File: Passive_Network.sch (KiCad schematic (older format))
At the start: 140 parts, among them J18 CONN_01X03, J19 CONN_01X03, J20 CONN_01X08, SW2 SW_Rotary3x4, X1 P7002SCLRP, X2 P7002SCLRP, X3 P7002SCLRP, X4 P7002SCLRP, X5 P7002SCLRP, X6 P7002SCLRP

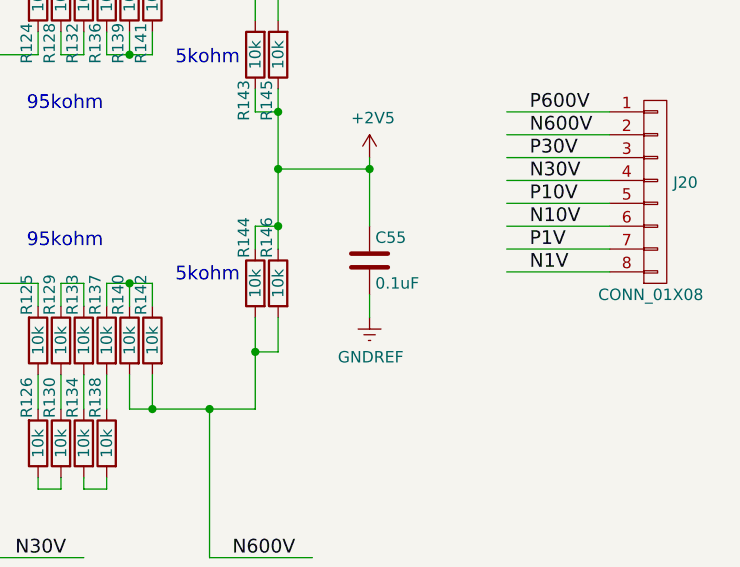
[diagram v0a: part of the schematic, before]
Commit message: 전해콘덴서 foot print 변경
전해 콘덴서 변경
Bypass 콘데서 OPAMP에 추가 하여야 함
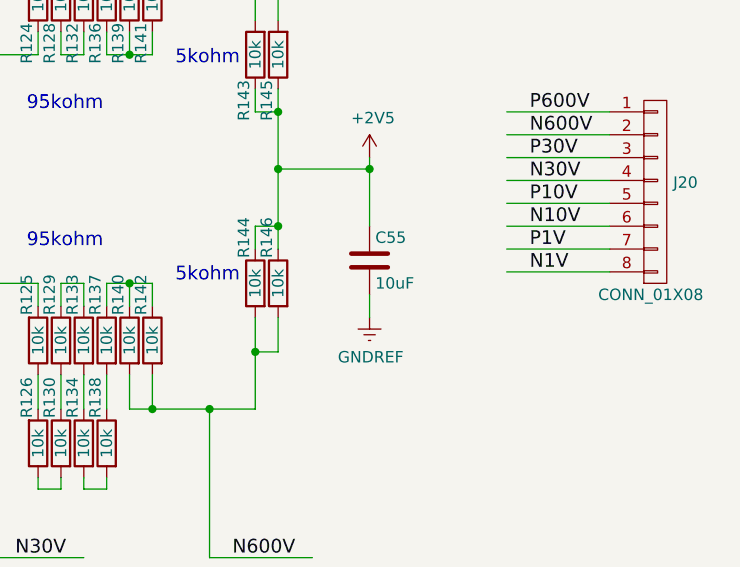
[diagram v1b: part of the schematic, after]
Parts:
- C55: value 0.1uF -> 10uF
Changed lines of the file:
@@
 P 9400 3300
 F 0 "C55" H 9425 3400 50  0000 L CNN
-F 1 "0.1uF" H 9425 3200 50  0000 L CNN
+F 1 "10uF" H 9425 3200 50  0000 L CNN
 F 2 "Capacitors_SMD:C_1210_HandSoldering" H 9438 3150 50  0001 C CNN
 F 3 "" H 9400 3300 50  0001 C CNN

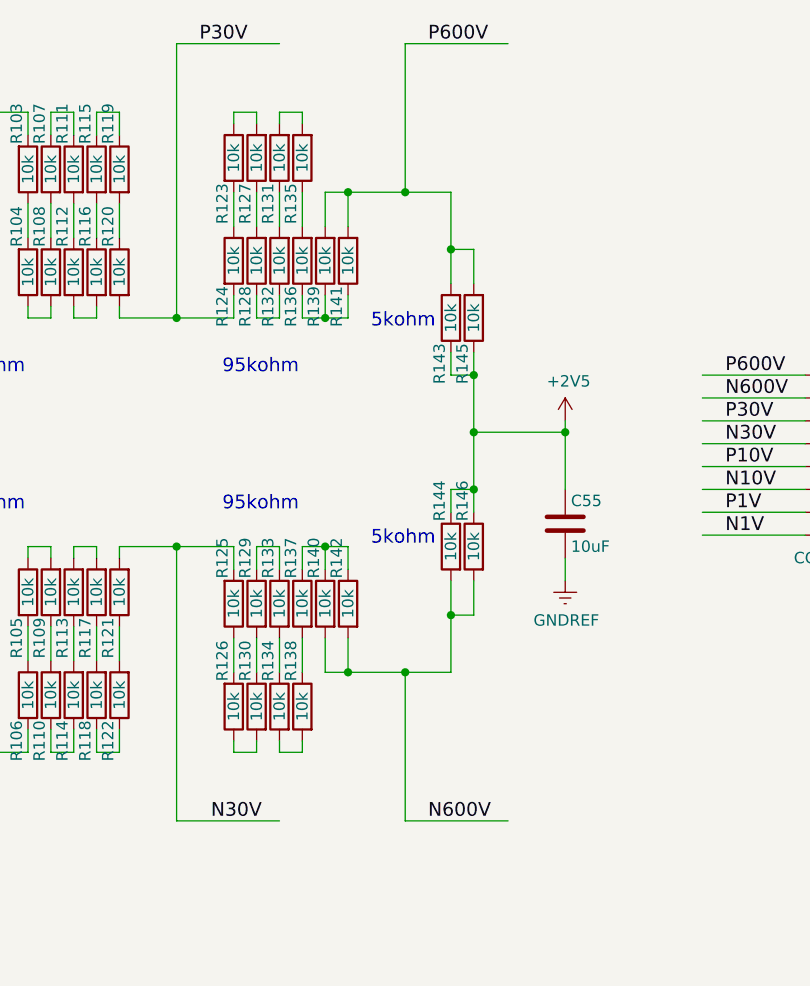
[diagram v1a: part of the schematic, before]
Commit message: 2차 PCB 1차 수정
1. ADR455 Vcc V12 수정
2. DCDC 입력전압 변경
3. Bypass 콘덴서 C66, C67 추가
4. SOIC 방향 표시
5. TLV431 PADS 변경
6. AQV258 Pin3 --> Pin2
7. 전해콘덴서 방향추가
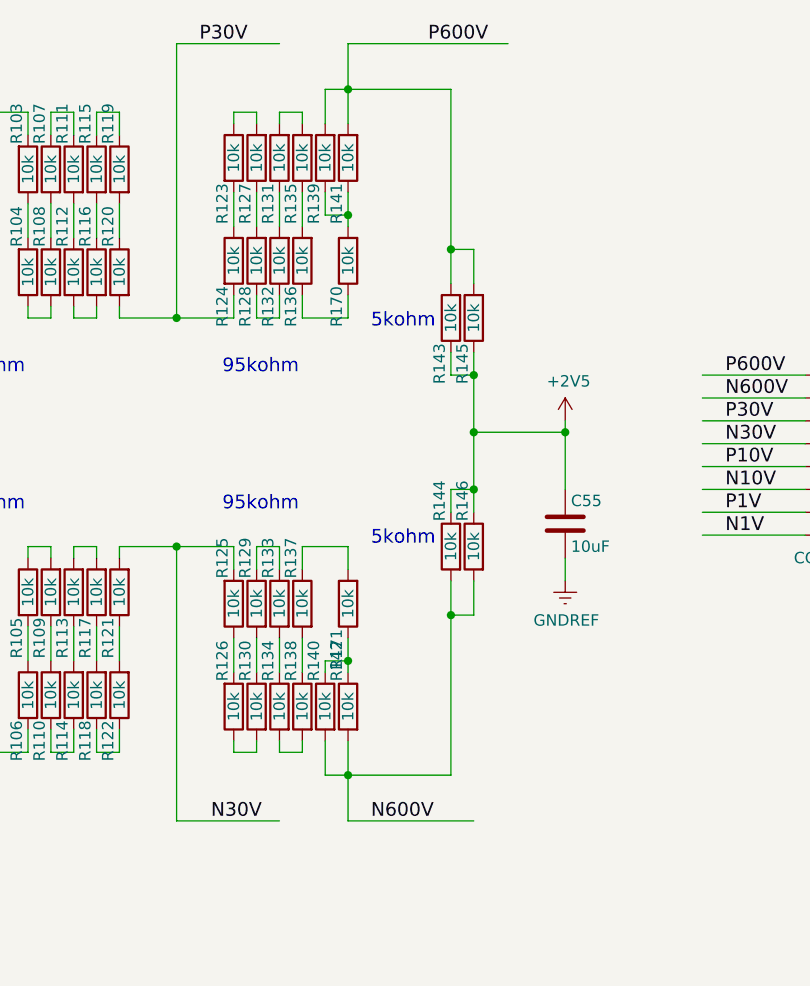
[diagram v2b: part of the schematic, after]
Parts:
- added R170, R171: 10k, Resistors_SMD:R_0805_HandSoldering, symbol R
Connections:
- wire segments 327 -> 329
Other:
- moved on the sheet: R139, R140, R141, R142
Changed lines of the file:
@@
 P30V
 Wire Wire Line
-	8700 1850 8700 1200
-Wire Wire Line
-	8700 1200 9150 1200
+	8450 1200 9150 1200
 Text Label 8800 1200 0    60   ~ 0
 P600V
@@
 Text Label 7850 4600 0    60   ~ 0
 N30V
-Text Label 8800 4600 0    60   ~ 0
+Text Label 8550 4600 0    60   ~ 0
 N600V
 Text Label 6300 4600 0    60   ~ 0
@@
 Text Label 6750 5750 0    60   ~ 0
 Monitor
-Connection ~ 8700 1850
 $Comp
 L C C55
@@
 L R R139
 U 1 1 5B0CFCAF
-P 8350 2150
-F 0 "R139" V 8400 2350 50  0000 C CNN
-F 1 "10k" V 8350 2150 50  0000 C CNN
-F 2 "Resistors_SMD:R_0805_HandSoldering" V 8280 2150 50  0001 C CNN
-F 3 "" H 8350 2150 50  0001 C CNN
-	1    8350 2150
+P 8350 1700
+F 0 "R139" V 8400 1900 50  0000 C CNN
+F 1 "10k" V 8350 1700 50  0000 C CNN
+F 2 "Resistors_SMD:R_0805_HandSoldering" V 8280 1700 50  0001 C CNN
+F 3 "" H 8350 1700 50  0001 C CNN
+	1    8350 1700
 	-1   0    0    1
 $EndComp
@@
 Wire Wire Line
 	8250 2300 8250 2400
-Wire Wire Line
-	8350 2400 8350 2300
 $Comp
 L R R123
@@
 L R R141
 U 1 1 5B0CFCDA
-P 8450 2150
-F 0 "R141" V 8500 2350 50  0000 C CNN
-F 1 "10k" V 8450 2150 50  0000 C CNN
-F 2 "Resistors_SMD:R_0805_HandSoldering" V 8380 2150 50  0001 C CNN
-F 3 "" H 8450 2150 50  0001 C CNN
-	1    8450 2150
+P 8450 1700
+F 0 "R141" V 8500 1900 50  0000 C CNN
+F 1 "10k" V 8450 1700 50  0000 C CNN
+F 2 "Resistors_SMD:R_0805_HandSoldering" V 8380 1700 50  0001 C CNN
+F 3 "" H 8450 1700 50  0001 C CNN
+	1    8450 1700
 	-1   0    0    1
 $EndComp
@@
 	8250 1500 8250 1550
 Wire Wire Line
-	8350 2000 8350 1850
+	8350 1550 8350 1400
 Wire Wire Line
 	7950 2400 7950 2300
@@
 Wire Wire Line
 	8450 2400 8450 2300
-Connection ~ 8350 2400
-Wire Wire Line
-	8350 1850 8900 1850
-Wire Wire Line
-	8450 1850 8450 2000
+Wire Wire Line
+	8450 1200 8450 1550
 $Comp
 L R R143
@@
 $EndComp
 Wire Wire Line
-	8900 1850 8900 2250
+	8900 1400 8900 2250
 Wire Wire Line
 	9000 2650 8900 2650
@@
 	9000 2100 9000 2250
 Connection ~ 8900 2100
-Connection ~ 8450 1850
+Connection ~ 8450 1400
 Connection ~ 9000 2650
 Text Notes 8550 2450 0    60   ~ 0
@@
 	7700 4600 8150 4600
 Connection ~ 7700 3400
-Wire Wire Line
-	8700 3950 8700 4600
-Wire Wire Line
-	8700 4600 9150 4600
 $Comp
 L R R23
@@
 	3850 4550 4300 4550
 Connection ~ 3850 4250
-Connection ~ 8700 3950
 $Comp
 L R R27
@@
 L R R140
 U 1 1 5B0D5F95
-P 8350 3650
-F 0 "R140" V 8400 3850 50  0000 C CNN
-F 1 "10k" V 8350 3650 50  0000 C CNN
-F 2 "Resistors_SMD:R_0805_HandSoldering" V 8280 3650 50  0001 C CNN
-F 3 "" H 8350 3650 50  0001 C CNN
-	1    8350 3650
+P 8350 4100
+F 0 "R140" V 8400 4300 50  0000 C CNN
+F 1 "10k" V 8350 4100 50  0000 C CNN
+F 2 "Resistors_SMD:R_0805_HandSoldering" V 8280 4100 50  0001 C CNN
+F 3 "" H 8350 4100 50  0001 C CNN
+	1    8350 4100
 	-1   0    0    -1
 $EndComp
@@
 Wire Wire Line
 	8250 3500 8250 3400
-Wire Wire Line
-	8350 3400 8350 3500
 $Comp
 L R R126
@@
 L R R142
 U 1 1 5B0D5FC0
-P 8450 3650
-F 0 "R142" V 8500 3850 50  0000 C CNN
-F 1 "10k" V 8450 3650 50  0000 C CNN
-F 2 "Resistors_SMD:R_0805_HandSoldering" V 8380 3650 50  0001 C CNN
-F 3 "" H 8450 3650 50  0001 C CNN
-	1    8450 3650
+P 8450 4100
+F 0 "R142" V 8500 4300 50  0000 C CNN
+F 1 "10k" V 8450 4100 50  0000 C CNN
+F 2 "Resistors_SMD:R_0805_HandSoldering" V 8380 4100 50  0001 C CNN
+F 3 "" H 8450 4100 50  0001 C CNN
+	1    8450 4100
 	-1   0    0    -1
 $EndComp
@@
 	8250 4300 8250 4250
 Wire Wire Line
-	8350 3800 8350 3950
+	8350 4250 8350 4400
 Wire Wire Line
 	7950 3400 7950 3500
@@
 Wire Wire Line
 	8450 3400 8450 3500
-Connection ~ 8350 3400
-Wire Wire Line
-	8350 3950 8900 3950
-Wire Wire Line
-	8450 3950 8450 3800
 $Comp
 L R R144
@@
 $EndComp
 Wire Wire Line
-	8900 3950 8900 3550
-Wire Wire Line
 	8900 3150 9000 3150
 Wire Wire Line
@@
 	9000 3700 9000 3550
 Connection ~ 8900 3700
-Connection ~ 8450 3950
+Connection ~ 8450 4400
 Connection ~ 9000 3150
 Text Notes 8550 3400 0    60   ~ 0
@@
 Wire Wire Line
 	1350 2900 1400 2900
+$Comp
+L R R170
+U 1 1 5B1D8CAE
+P 8450 2150
+F 0 "R170" V 8500 2350 50  0000 C CNN
+F 1 "10k" V 8450 2150 50  0000 C CNN
+F 2 "Resistors_SMD:R_0805_HandSoldering" V 8380 2150 50  0001 C CNN
+F 3 "" H 8450 2150 50  0001 C CNN
+	1    8450 2150
+	-1   0    0    1
+$EndComp
+Wire Wire Line
+	8350 1850 8350 1950
+Wire Wire Line
+	8350 1950 8450 1950
+Wire Wire Line
+	8450 1850 8450 2000
+Connection ~ 8450 1950
+Wire Wire Line
+	8350 1400 8900 1400
+$Comp
+L R R171
+U 1 1 5B1DBB59
+P 8450 3650
+F 0 "R171" V 8500 3850 50  0000 C CNN
+F 1 "10k" V 8450 3650 50  0000 C CNN
+F 2 "Resistors_SMD:R_0805_HandSoldering" V 8380 3650 50  0001 C CNN
+F 3 "" H 8450 3650 50  0001 C CNN
+	1    8450 3650
+	-1   0    0    1
+$EndComp
+Wire Wire Line
+	8450 3800 8450 3950
+Wire Wire Line
+	8450 3900 8350 3900
+Wire Wire Line
+	8350 3900 8350 3950
+Connection ~ 8450 3900
+Wire Wire Line
+	8450 4600 9000 4600
+Wire Wire Line
+	8350 4400 8900 4400
+Wire Wire Line
+	8450 4250 8450 4600
+Wire Wire Line
+	8900 4400 8900 3550
 $EndSCHEMATC

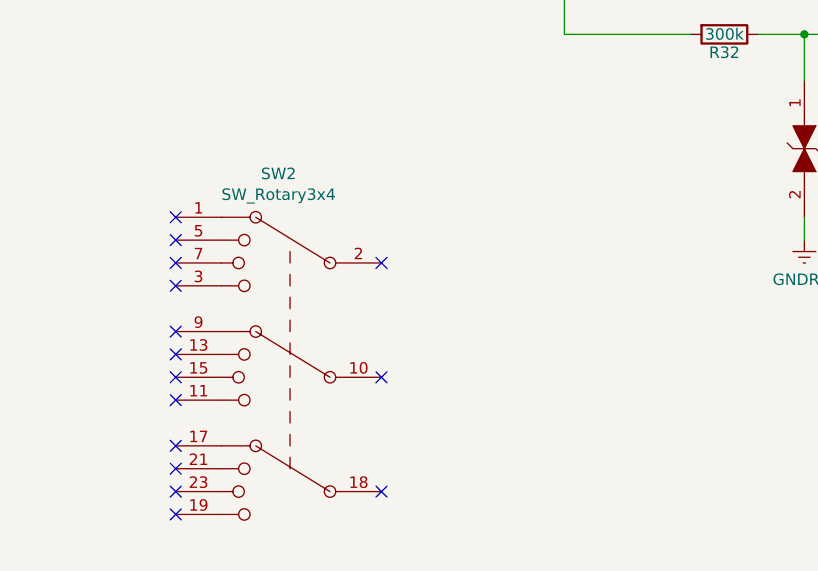
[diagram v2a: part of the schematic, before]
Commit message: Selector 표시
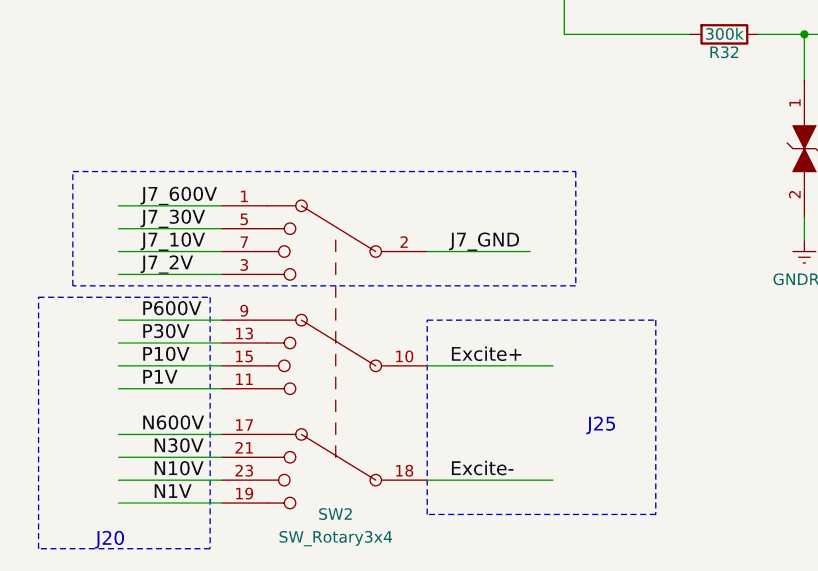
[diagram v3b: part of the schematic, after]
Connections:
- net labels added: Excite+, Excite-, J7_10V, J7_2V, J7_30V, J7_600V, J7_GND
- wire segments 329 -> 344
- no-connect marks 15 -> 0
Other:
- note added: "J20\n"
- note added: "J25"
- moved on the sheet: SW2
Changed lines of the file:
@@
 L SW_Rotary3x4 SW2
 U 1 1 5B044819
-P 2000 6600
-F 0 "SW2" H 2050 7490 50  0000 C CNN
-F 1 "SW_Rotary3x4" H 2050 7399 50  0000 C CNN
-F 2 "" H 1900 7400 50  0001 C CNN
-F 3 "" H 1900 7400 50  0001 C CNN
-	1    2000 6600
+P 2200 6550
+F 0 "SW2" H 2200 5900 50  0000 C CNN
+F 1 "SW_Rotary3x4" H 2200 5800 50  0000 C CNN
+F 2 "" H 2100 7350 50  0001 C CNN
+F 3 "" H 2100 7350 50  0001 C CNN
+	1    2200 6550
 	-1   0    0    -1
 $EndComp
@@
 	1    0    0    1
 $EndComp
-NoConn ~ 1500 5900
-NoConn ~ 1500 6000
-NoConn ~ 1500 6100
-NoConn ~ 1500 6200
-NoConn ~ 1500 6400
-NoConn ~ 1500 6500
-NoConn ~ 1500 6600
-NoConn ~ 1500 6700
-NoConn ~ 1500 6900
-NoConn ~ 1500 7000
-NoConn ~ 1500 7100
-NoConn ~ 1500 7200
-NoConn ~ 2400 7100
-NoConn ~ 2400 6100
-NoConn ~ 2400 6600
 $Comp
 L DIAC X5
@@
 Wire Wire Line
 	8900 4400 8900 3550
+Text Label 1400 6950 0    60   ~ 0
+N30V
+Text Label 1350 6850 0    60   ~ 0
+N600V
+Text Label 1400 7050 0    60   ~ 0
+N10V
+Text Label 1400 7150 0    60   ~ 0
+N1V
+Wire Wire Line
+	1250 7050 1700 7050
+Wire Wire Line
+	1250 6950 1700 6950
+Wire Wire Line
+	1250 7150 1700 7150
+Wire Wire Line
+	1250 6850 1700 6850
+Wire Wire Line
+	1250 6550 1700 6550
+Wire Wire Line
+	1250 6450 1700 6450
+Text Label 1350 6450 0    60   ~ 0
+P30V
+Wire Wire Line
+	1250 6350 1700 6350
+Text Label 1350 6350 0    60   ~ 0
+P600V
+Text Label 1350 6550 0    60   ~ 0
+P10V
+Wire Wire Line
+	1250 6650 1700 6650
+Text Label 1350 6650 0    60   ~ 0
+P1V
+Text Label 2700 6550 0    60   ~ 0
+Excite+
+Text Label 2700 7050 0    60   ~ 0
+Excite-
+Wire Wire Line
+	2600 7050 3150 7050
+Wire Wire Line
+	2600 6550 3150 6550
+Wire Wire Line
+	2600 6050 3050 6050
+Text Label 2700 6050 0    60   ~ 0
+J7_GND
+Wire Wire Line
+	1250 5850 1700 5850
+Text Label 1350 5850 0    60   ~ 0
+J7_600V
+Wire Wire Line
+	1250 5950 1700 5950
+Text Label 1350 5950 0    60   ~ 0
+J7_30V
+Wire Wire Line
+	1250 6050 1700 6050
+Text Label 1350 6050 0    60   ~ 0
+J7_10V
+Wire Wire Line
+	1250 6150 1700 6150
+Text Label 1350 6150 0    60   ~ 0
+J7_2V
+Wire Notes Line
+	900  6250 1650 6250
+Wire Notes Line
+	1650 6250 1650 7350
+Wire Notes Line
+	1650 7350 900  7350
+Wire Notes Line
+	900  7350 900  6250
+Wire Notes Line
+	2600 6350 3600 6350
+Wire Notes Line
+	3600 6350 3600 7200
+Wire Notes Line
+	3600 7200 2600 7200
+Wire Notes Line
+	2600 7200 2600 6350
+Wire Notes Line
+	1050 5700 3250 5700
+Wire Notes Line
+	3250 5700 3250 6200
+Wire Notes Line
+	3250 6200 1050 6200
+Wire Notes Line
+	1050 6200 1050 5700
+Text Notes 1150 7350 0    60   ~ 0
+J20\n
+Text Notes 3300 6850 0    60   ~ 0
+J25
 $EndSCHEMATC

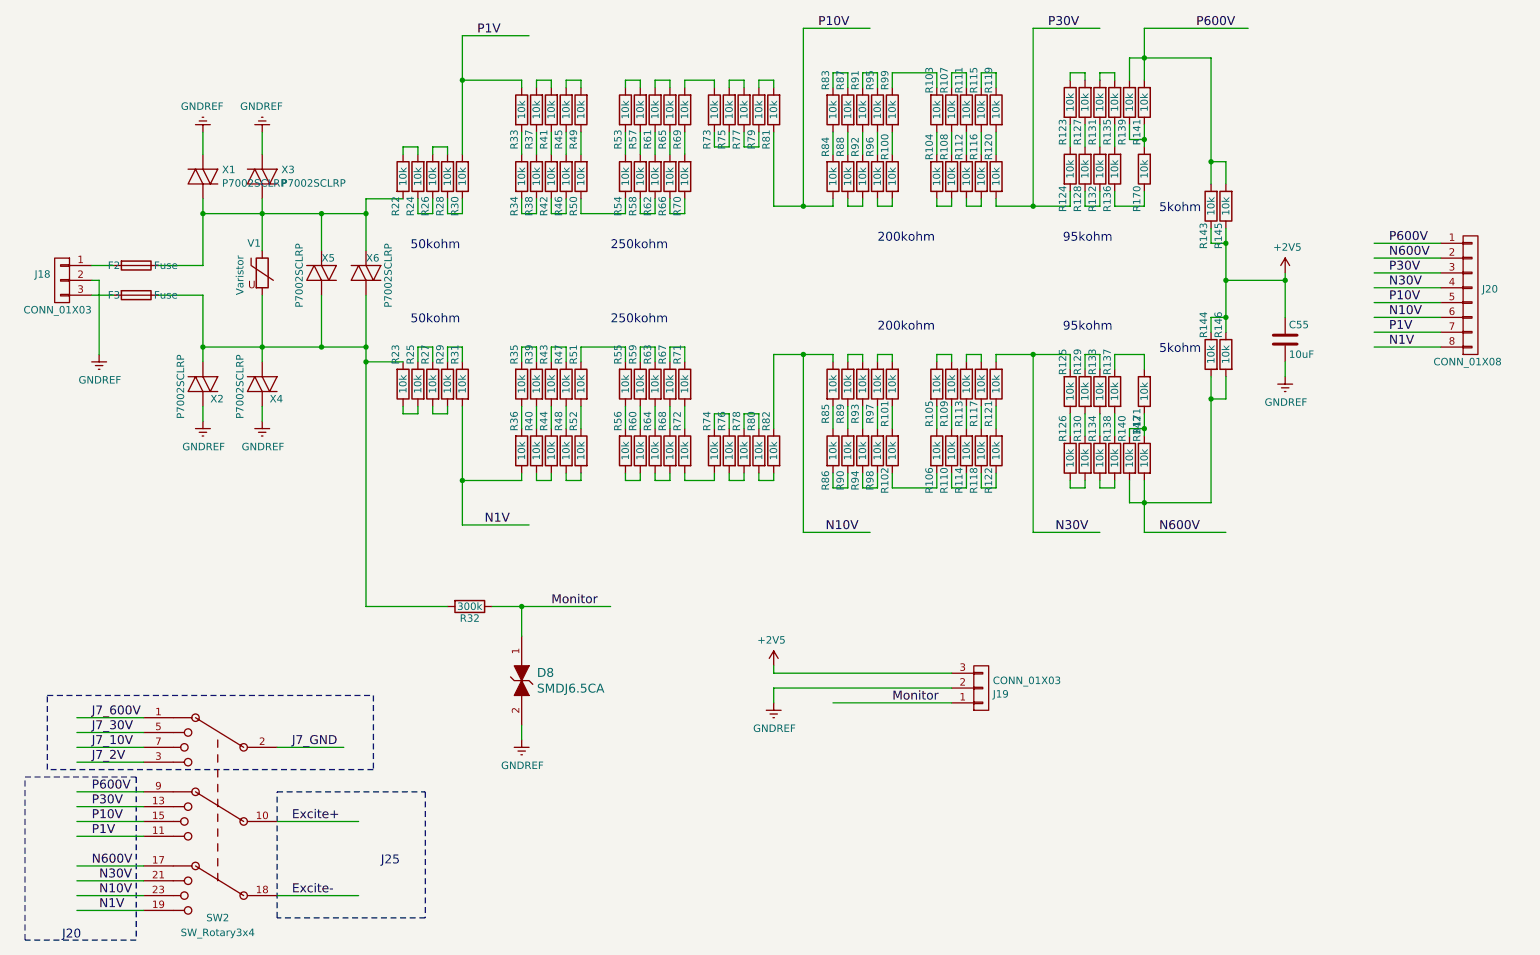
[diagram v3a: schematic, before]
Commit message: Selector Numbering
Selector numbering
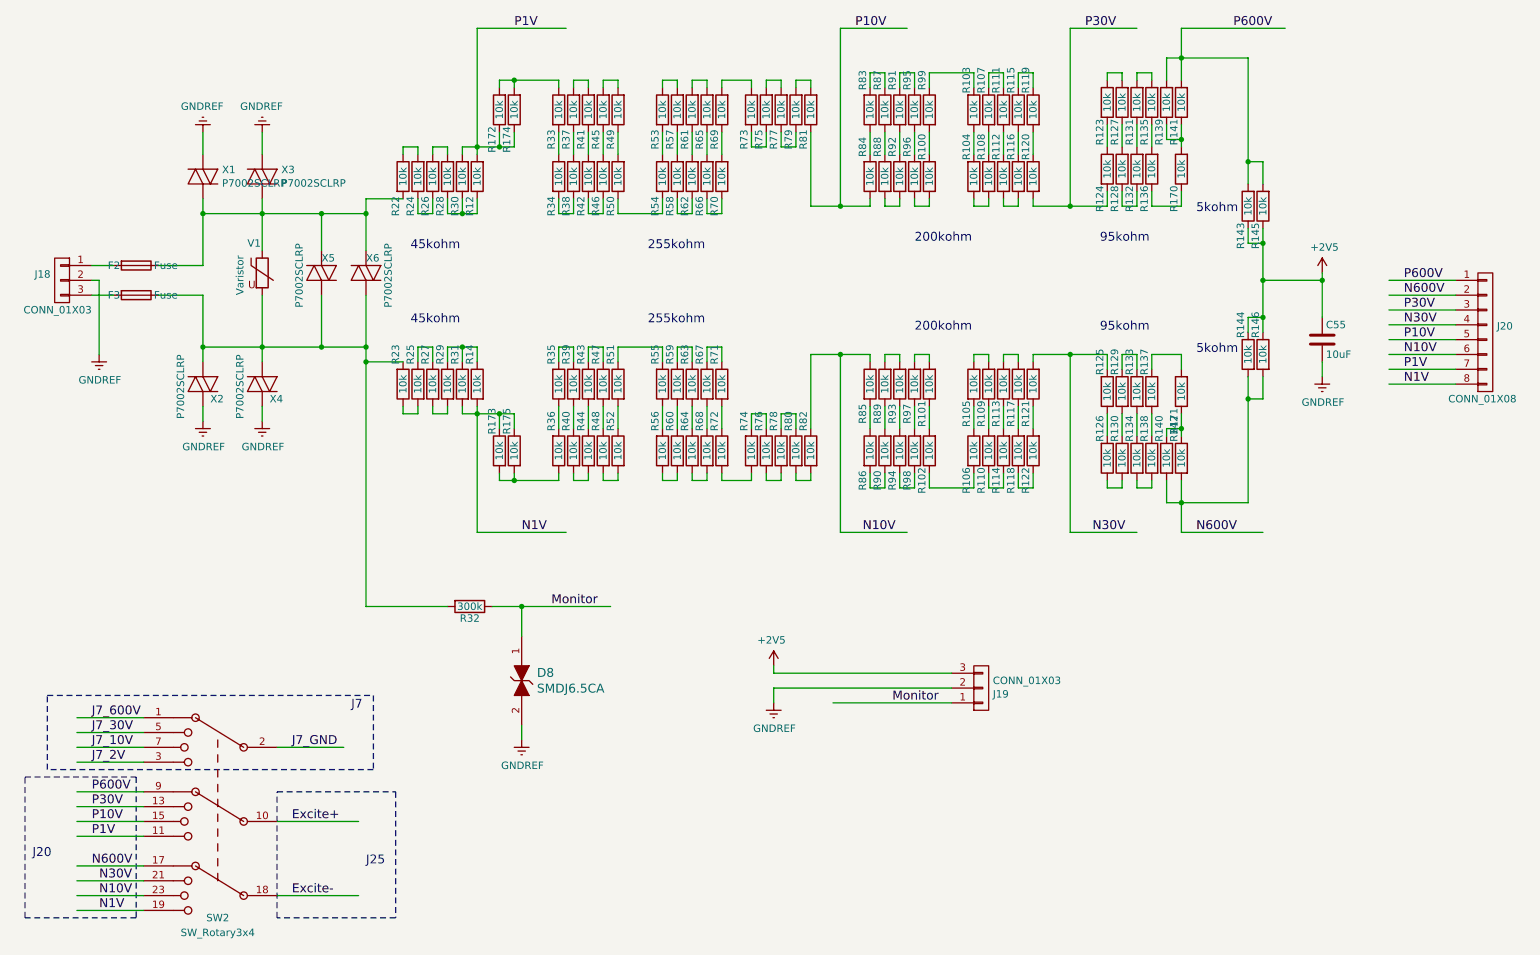
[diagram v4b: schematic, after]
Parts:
- added R12, R14, R172, R173, R174, R175: 10k, Resistors_SMD:R_0805_HandSoldering, symbol R
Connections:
- wire segments 344 -> 358
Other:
- note added: "255kohm\n"
- note added: "45kohm\n"
- note added: "J7\n"
- note removed: "250kohm\n"
- note removed: "50kohm\n"
- moved on the sheet: C55, J20, R100, R101, R102, R103, R104, R105, R106, R107, R108, R109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

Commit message: 0805_넓히기
기타 수정
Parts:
- R100, R101, R102, R103, R104, R105, R106, R107, R108, R109, R110, R111, R112, R113, R114, R115, R116, R117, R118, R119, R12, R120, R121, R122, R123, R124, R125, R126, R127, R128, R129, R130, R131, R132, R133, R134, R135, R136, R137, R138, R139, R140, R141, R142, R143, R144, R145, R146, R170, R171, R172, R173, R174, R175, R22, R23, R24, R25, R26, R27, R28, R29, R30, R31, R33, R34, R35, R36, R37, R38, R39, R40, R41, R42, R43, R44, R45, R46, R47, R48, R49, R50, R51, R52, R53, R54, R55, R56, R57, R58, R59, R60, R61, R62, R63, R64, R65, R66, R67, R68, R69, R70, R71, R72, R73, R74, R75, R76, R77, R78, R79, R80, R81, R82, R83, R84, R85, R86, R87, R88, R89, R90, R91, R92, R93, R94, R95, R96, R97, R98, R99: footprint Resistors_SMD:R_0805_HandSoldering -> USER:R_0805_HandSoldering_long

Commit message: 1206 update
다시 보세요.
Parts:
- R100, R101, R102, R103, R104, R105, R106, R107, R108, R109, R110, R111, R112, R113, R114, R115, R116, R117, R118, R119, R12, R120, R121, R122, R123, R124, R125, R126, R127, R128, R129, R130, R131, R132, R133, R134, R135, R136, R137, R138, R139, R140, R141, R142, R143, R144, R145, R146, R170, R171, R172, R173, R174, R175, R22, R23, R24, R25, R26, R27, R28, R29, R30, R31, R33, R34, R35, R36, R37, R38, R39, R40, R41, R42, R43, R44, R45, R46, R47, R48, R49, R50, R51, R52, R53, R54, R55, R56, R57, R58, R59, R60, R61, R62, R63, R64, R65, R66, R67, R68, R69, R70, R71, R72, R73, R74, R75, R76, R77, R78, R79, R80, R81, R82, R83, R84, R85, R86, R87, R88, R89, R90, R91, R92, R93, R94, R95, R96, R97, R98, R99: footprint USER:R_0805_HandSoldering_long -> Resistors_SMD:R_1206_HandSoldering
